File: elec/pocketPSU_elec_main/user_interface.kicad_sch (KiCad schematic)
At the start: 0 parts

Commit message: added user interface elements
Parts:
- added C1: C_Small, symbol Device:C_Small
- added C2, C3: 10nF, symbol Device:C_Small
- added J1: Conn_01x12_MountingPin, footprints:LCD-GMT020-02, symbol Connector_Generic_MountingPin:Conn_01x12_MountingPin
- added KEY1, KEY2, KEY3: TS3325A 250GF 025, footprints:KEY-SMD_4P-L3.1-W3.1-P2.00-LS4.0, symbol footprints:TS3325A250GF025
- added R1: 4.7R, symbol Device:R_Small
- added R2, R3, R4, R5, R6, R7, R8, R9: 10K, symbol Device:R_Small
- added SW1: EC11E09244BS, footprints:SW-TH_EC11XXXXXXXX, symbol footprints:EC11E09244BS
- added U1: 2N7002_C5224215, footprints:SOT-23-3_L3.0-W1.6-P1.90-LS2.8-BR, symbol footprints:2N7002_C5224215
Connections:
- new net: C2.1, R2.2, R3.2, SW1.A
- new net: C3.1, R4.2, R5.1, SW1.B
- new net: R1.2, U1.3 (D)
- new net +3.3V: C1.1, J1.3 (Pin_3), J1.4 (Pin_4), R2.1, R4.1, R6.1, R7.1, R8.1, R9.1
- new net BT_1: KEY1.1, KEY1.2, R7.2
- new net BT_2: KEY2.1, KEY2.2, R8.2
- new net BT_3: KEY3.1, KEY3.2, R9.2
- new net ENCODER_A: R3.1
- new net ENCODER_B: R5.2
- new net ENCODER_BT: R6.2, SW1.D
- new net GND: C1.2, C2.2, C3.2, J1.1 (Pin_1), J1.12 (Pin_12), J1.5 (Pin_5), J1.6 (Pin_6), KEY1.3, KEY1.4, KEY1.5, KEY1.6, KEY2.3, KEY2.4, KEY2.5, KEY2.6, KEY3.3, KEY3.4, KEY3.5, KEY3.6, SW1.6, SW1.7, SW1.C, SW1.E, U1.2 (S)
- new net LEDK: J1.2 (Pin_2), R1.1
- new net SCREEN_BACKLIGHT_EN: U1.1 (G)
- new net SPI_CS: J1.8 (Pin_8)
- new net SPI_DC: J1.7 (Pin_7)
- new net SPI_MOSI: J1.10 (Pin_10)
- new net SPI_RESET: J1.11 (Pin_11)
- new net SPI_SCK: J1.9 (Pin_9)

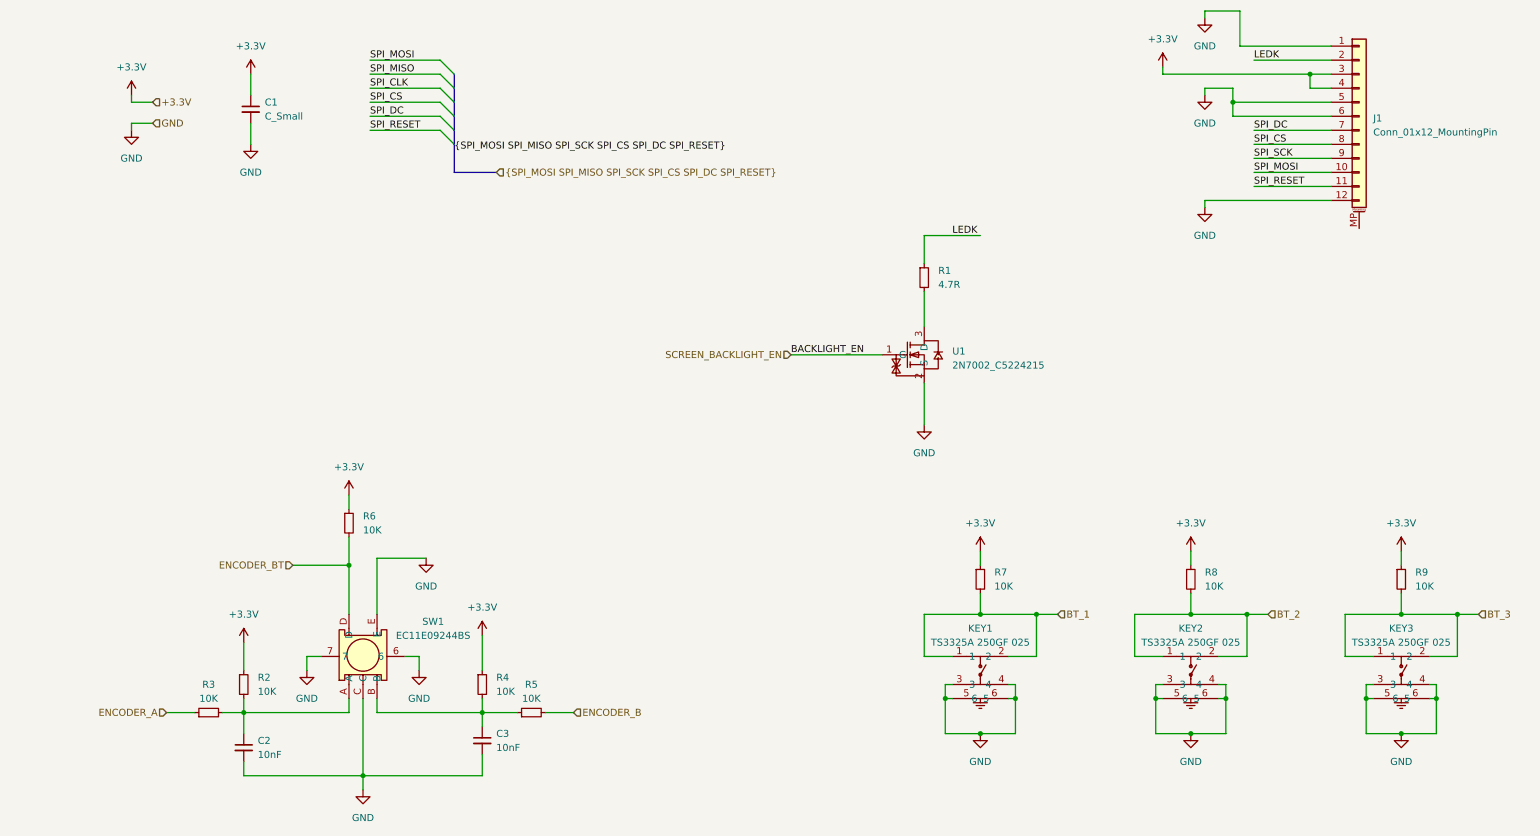
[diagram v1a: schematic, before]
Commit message: add button, deglitch
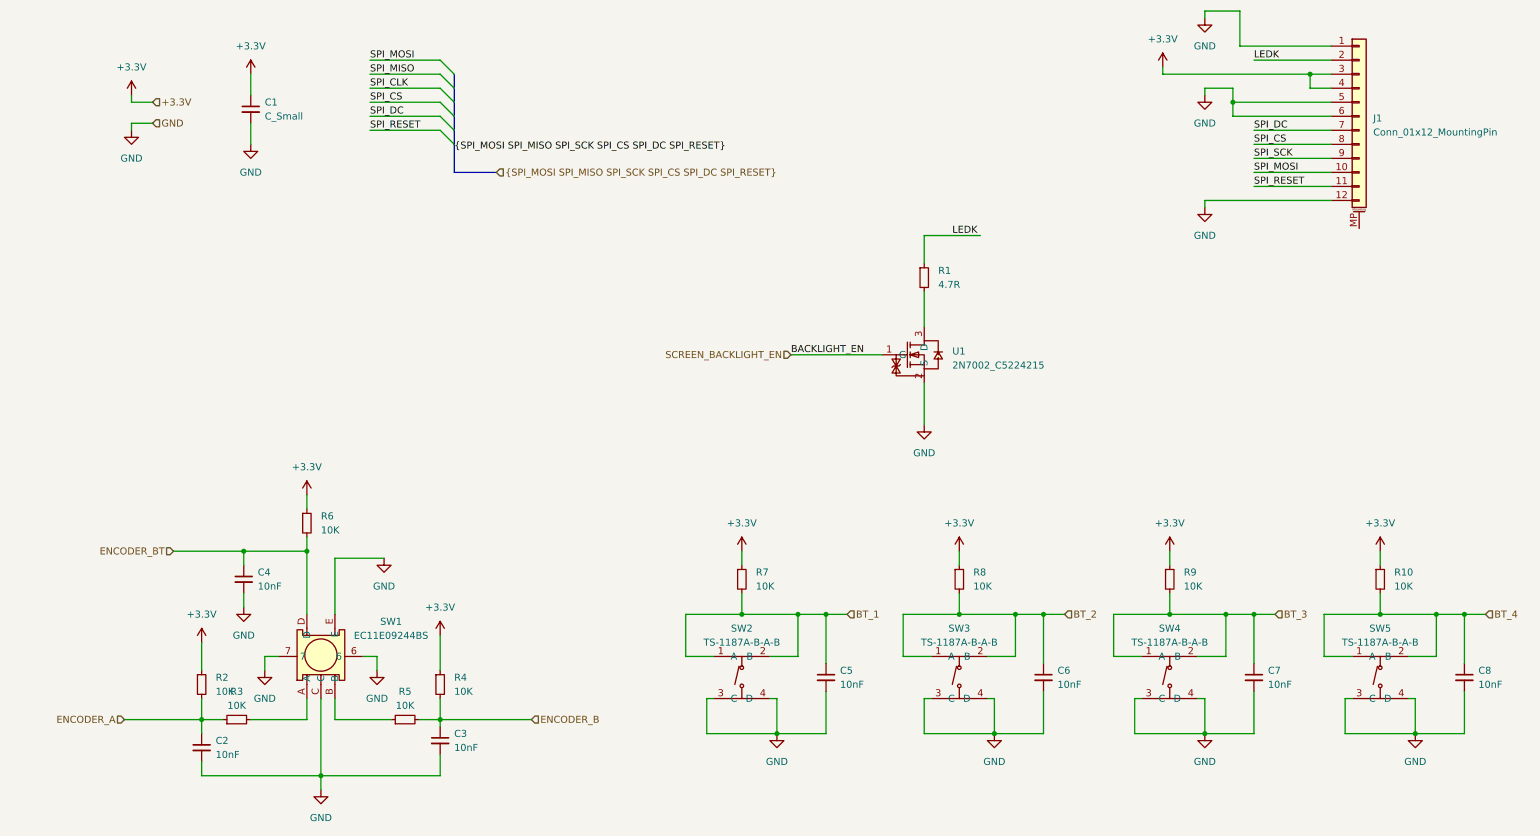
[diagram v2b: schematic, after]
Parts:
- removed KEY1, KEY2, KEY3: TS3325A 250GF 025, footprints:KEY-SMD_4P-L3.1-W3.1-P2.00-LS4.0, symbol footprints:TS3325A250GF025
- added C4, C5, C6, C7, C8: 10nF, symbol Device:C_Small
- added R10: 10K, symbol Device:R_Small
- added SW2, SW3, SW4, SW5: TS-1187A-B-A-B, footprints:SW-SMD_4P-L5.1-W5.1-P3.70-LS6.5-TL-2, symbol footprints:TS-1187A-B-A-B
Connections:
- net +3.3V: now also R10.1
- net BT_1: now also C5.1, SW2.1 (A), SW2.2 (B)
- net BT_2: now also C6.1, SW3.1 (A), SW3.2 (B)
- net BT_3: now also C7.1, SW4.1 (A), SW4.2 (B)
- net ENCODER_A: now also C2.1, R2.2
- net ENCODER_B: now also C3.1, R4.2
- net ENCODER_BT: now also C4.1
- net GND: now also C4.2, C5.2, C6.2, C7.2, C8.2, SW2.3 (C), SW2.4 (D), SW3.3 (C), SW3.4 (D), SW4.3 (C), SW4.4 (D), SW5.3 (C), SW5.4 (D)
- net at R3.2, SW1.A: no longer C2.1, R2.2
- net at R5.1, SW1.B: no longer C3.1, R4.2
- new net BT_4: C8.1, R10.2, SW5.1 (A), SW5.2 (B)
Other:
- moved on the sheet: C2, C3, R2, R3, R4, R5, R6, R7, SW1

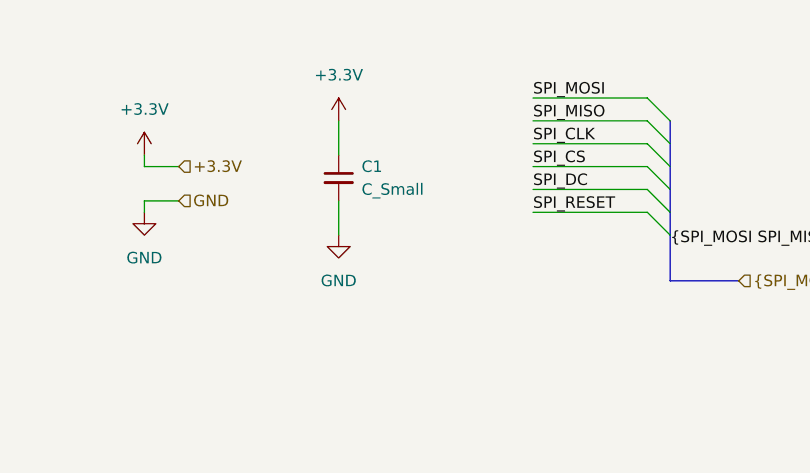
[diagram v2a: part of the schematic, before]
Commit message: add value to bypass cap
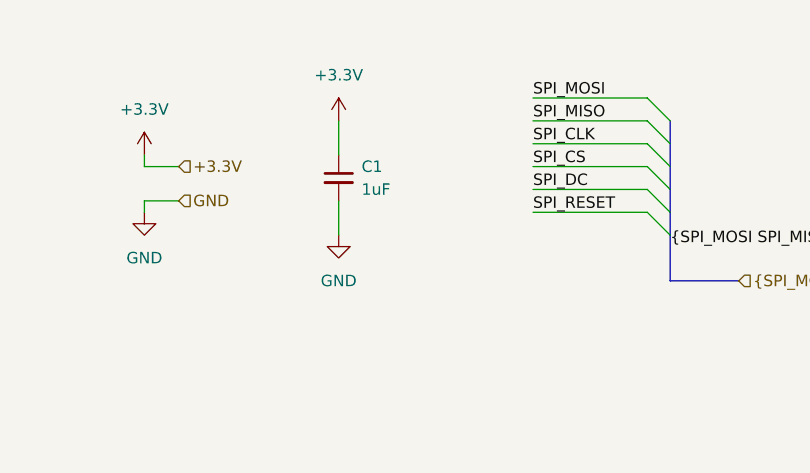
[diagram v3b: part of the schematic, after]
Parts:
- C1: value C_Small -> 1uF
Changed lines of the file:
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@@
 			)
 		)
-		(property "Value" "C_Small"
+		(property "Value" "1uF"
 			(at 57.15 41.9162 0)
 			(effects

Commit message: add esp32 micro
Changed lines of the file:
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@@
 	)
 	(hierarchical_label "ENCODER_BT"
-		(shape input)
+		(shape output)
 		(at 40.64 120.65 180)
 		(fields_autoplaced yes)
@@
 	)
 	(hierarchical_label "ENCODER_A"
-		(shape input)
+		(shape output)
 		(at 31.75 151.13 180)
 		(fields_autoplaced yes)
@@
 	)
 	(hierarchical_label "BT_3"
-		(shape input)
+		(shape output)
 		(at 240.03 132.08 0)
 		(fields_autoplaced yes)
@@
 	)
 	(hierarchical_label "BT_1"
-		(shape input)
+		(shape output)
 		(at 162.56 132.08 0)
 		(fields_autoplaced yes)
@@
 	)
 	(hierarchical_label "ENCODER_B"
-		(shape input)
+		(shape output)
 		(at 105.41 151.13 0)
 		(fields_autoplaced yes)
@@
 	)
 	(hierarchical_label "BT_4"
-		(shape input)
+		(shape output)
 		(at 278.13 132.08 0)
 		(fields_autoplaced yes)
@@
 	)
 	(hierarchical_label "BT_2"
-		(shape input)
+		(shape output)
 		(at 201.93 132.08 0)
 		(fields_autoplaced yes)

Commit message: preliminary layout
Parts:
- C1: footprint (none) -> Resistor_SMD:R_0805_2012Metric
- C2, C3, C4, C5, C6, C7, C8: footprint (none) -> Capacitor_SMD:C_0402_1005Metric
- R1, R10, R2, R3, R4, R5, R6, R7, R8, R9: footprint (none) -> Resistor_SMD:R_0402_1005Metric
- renumbered SW3 to BTDOWN1, SW5 to BTON1, SW4 to BTSELECT1, SW2 to BTUP1
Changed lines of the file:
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@@
 			)
 		)
-		(property "Footprint" ""
+		(property "Footprint" "Resistor_SMD:R_0805_2012Metric"
 			(at 54.61 40.64 0)
 			(effects
@@
 			)
 		)
-		(property "Footprint" ""
+		(property "Footprint" "Capacitor_SMD:C_0402_1005Metric"
 			(at 236.22 143.51 0)
 			(effects
@@
 			)
 		)
-		(property "Footprint" ""
+		(property "Footprint" "Resistor_SMD:R_0402_1005Metric"
 			(at 45.72 144.78 0)
 			(effects
@@
 			)
 		)
-		(property "Footprint" ""
+		(property "Footprint" "Resistor_SMD:R_0402_1005Metric"
 			(at 82.55 151.13 0)
 			(effects
@@
 			)
 		)
-		(property "Footprint" ""
+		(property "Footprint" "Resistor_SMD:R_0402_1005Metric"
 			(at 220.98 125.73 0)
 			(effects
@@
 		(dnp no)
 		(fields_autoplaced yes)
-		(property "Reference" "SW5"
+		(property "Reference" "BTON1"
 			(at 259.08 134.62 0)
 			(effects
@@
 			(project "pocketPSU_elec_main"
 				(path "/439011d5-4dd5-4d65-a9bd-b0be402d54a5/cbe29d96-4bd9-4dd2-be02-96003f32f1da"
-					(reference "SW5")
+					(reference "BTON1")
 					(unit 1)
 				)
@@
 			)
 		)
-		(property "Footprint" ""
+		(property "Footprint" "Capacitor_SMD:C_0402_1005Metric"
 			(at 198.12 143.51 0)
 			(effects
@@
 		(dnp no)
 		(fields_autoplaced yes)
-		(property "Reference" "SW3"
+		(property "Reference" "BTDOWN1"
 			(at 182.88 134.62 0)
 			(effects
@@
 			(project "pocketPSU_elec_main"
 				(path "/439011d5-4dd5-4d65-a9bd-b0be402d54a5/cbe29d96-4bd9-4dd2-be02-96003f32f1da"
-					(reference "SW3")
+					(reference "BTDOWN1")
 					(unit 1)
 				)
@@
 			)
 		)
-		(property "Footprint" ""
+		(property "Footprint" "Capacitor_SMD:C_0402_1005Metric"
 			(at 158.75 143.51 0)
 			(effects
@@
 			)
 		)
-		(property "Footprint" ""
+		(property "Footprint" "Capacitor_SMD:C_0402_1005Metric"
 			(at 88.9 154.94 0)
 			(effects
@@
 			)
 		)
-		(property "Footprint" ""
+		(property "Footprint" "Resistor_SMD:R_0402_1005Metric"
 			(at 64.77 115.57 0)
 			(effects
@@
 			)
 		)
-		(property "Footprint" ""
+		(property "Footprint" "Capacitor_SMD:C_0402_1005Metric"
 			(at 53.34 125.73 0)
 			(effects
@@
 			)
 		)
-		(property "Footprint" ""
+		(property "Footprint" "Resistor_SMD:R_0402_1005Metric"
 			(at 176.53 71.12 0)
 			(effects
@@
 			)
 		)
-		(property "Footprint" ""
+		(property "Footprint" "Resistor_SMD:R_0402_1005Metric"
 			(at 143.51 125.73 0)
 			(effects
@@
 			)
 		)
-		(property "Footprint" ""
+		(property "Footprint" "Resistor_SMD:R_0402_1005Metric"
 			(at 88.9 144.78 0)
 			(effects
@@
 		(dnp no)
 		(fields_autoplaced yes)
-		(property "Reference" "SW4"
+		(property "Reference" "BTSELECT1"
 			(at 220.98 134.62 0)
 			(effects
@@
 			(project "pocketPSU_elec_main"
 				(path "/439011d5-4dd5-4d65-a9bd-b0be402d54a5/cbe29d96-4bd9-4dd2-be02-96003f32f1da"
-					(reference "SW4")
+					(reference "BTSELECT1")
 					(unit 1)
 				)
@@
 			)
 		)
-		(property "Footprint" ""
+		(property "Footprint" "Resistor_SMD:R_0402_1005Metric"
 			(at 182.88 125.73 0)
 			(effects
@@
 			)
 		)
-		(property "Footprint" ""
+		(property "Footprint" "Capacitor_SMD:C_0402_1005Metric"
 			(at 45.72 156.21 0)
 			(effects
@@
 			)
 		)
-		(property "Footprint" ""
+		(property "Footprint" "Resistor_SMD:R_0402_1005Metric"
 			(at 259.08 125.73 0)
 			(effects
@@
 			)
 		)
-		(property "Footprint" ""
+		(property "Footprint" "Resistor_SMD:R_0402_1005Metric"
 			(at 52.07 151.13 0)
 			(effects
@@
 		(dnp no)
 		(fields_autoplaced yes)
-		(property "Reference" "SW2"
+		(property "Reference" "BTUP1"
 			(at 143.51 134.62 0)
 			(effects
@@
 			(project "pocketPSU_elec_main"
 				(path "/439011d5-4dd5-4d65-a9bd-b0be402d54a5/cbe29d96-4bd9-4dd2-be02-96003f32f1da"
-					(reference "SW2")
+					(reference "BTUP1")
 					(unit 1)
 				)
@@
 			)
 		)
-		(property "Footprint" ""
+		(property "Footprint" "Capacitor_SMD:C_0402_1005Metric"
 			(at 274.32 143.51 0)
 			(effects

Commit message: add usb coms chip
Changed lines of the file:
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@@
-	(wire
-		(pts
-			(xy 33.02 43.18) (xy 36.83 43.18)
-		)
-		(stroke
-			(width 0)
-			(type default)
-		)
-	)
 	(wire
 		(pts
@@
 	(wire
 		(pts
-			(xy 33.02 39.37) (xy 36.83 39.37)
-		)
-		(stroke
-			(width 0)
-			(type default)
-		)
-	)
-	(wire
-		(pts
 			(xy 158.75 132.08) (xy 162.56 132.08)
 		)
@@
 	(wire
 		(pts
-			(xy 33.02 44.45) (xy 33.02 43.18)
-		)
-		(stroke
-			(width 0)
-			(type default)
-		)
-	)
-	(wire
-		(pts
 			(xy 45.72 137.16) (xy 45.72 142.24)
 		)
@@
 		(pts
 			(xy 264.16 139.7) (xy 269.24 139.7)
-		)
-		(stroke
-			(width 0)
-			(type default)
-		)
-	)
-	(wire
-		(pts
-			(xy 33.02 38.1) (xy 33.02 39.37)
 		)
 		(stroke
@@
 		(shape output)
 		(at 240.03 132.08 0)
-		(fields_autoplaced yes)
-		(effects
-			(font
-				(size 1.27 1.27)
-			)
-			(justify left)
-		)
-	)
-	(hierarchical_label "GND"
-		(shape input)
-		(at 36.83 43.18 0)
-		(fields_autoplaced yes)
-		(effects
-			(font
-				(size 1.27 1.27)
-			)
-			(justify left)
-		)
-	)
-	(hierarchical_label "+3.3V"
-		(shape input)
-		(at 36.83 39.37 0)
 		(fields_autoplaced yes)
 		(effects
@@
 	)
 	(symbol
-		(lib_id "power:+3.3V")
-		(at 33.02 38.1 0)
-		(unit 1)
-		(exclude_from_sim no)
-		(in_bom yes)
-		(on_board yes)
-		(dnp no)
-		(fields_autoplaced yes)
-		(property "Reference" "#PWR09"
-			(at 33.02 41.91 0)
-			(effects
-				(font
-					(size 1.27 1.27)
-				)
-				(hide yes)
-			)
-		)
-		(property "Value" "+3.3V"
-			(at 33.02 33.02 0)
-			(effects
-				(font
-					(size 1.27 1.27)
-				)
-			)
-		)
-		(property "Footprint" ""
-			(at 33.02 38.1 0)
-			(effects
-				(font
-					(size 1.27 1.27)
-				)
-				(hide yes)
-			)
-		)
-		(property "Datasheet" ""
-			(at 33.02 38.1 0)
-			(effects
-				(font
-					(size 1.27 1.27)
-				)
-				(hide yes)
-			)
-		)
-		(property "Description" "Power symbol creates a global label with name \"+3.3V\""
-			(at 33.02 38.1 0)
-			(effects
-				(font
-					(size 1.27 1.27)
-				)
-				(hide yes)
-			)
-		)
-		(pin "1"
-		)
-		(instances
-			(project "pocketPSU_elec_main"
-				(path "/439011d5-4dd5-4d65-a9bd-b0be402d54a5/cbe29d96-4bd9-4dd2-be02-96003f32f1da"
-					(reference "#PWR09")
-					(unit 1)
-				)
-			)
-		)
-	)
-	(symbol
 		(lib_id "Device:R_Small")
 		(at 45.72 144.78 0)
@@
 					(unit 1)
 				)
-			)
-		)
-	)
-	(symbol
-		(lib_id "power:GND")
-		(at 33.02 44.45 0)
-		(unit 1)
-		(exclude_from_sim no)
-		(in_bom yes)
-		(on_board yes)
-		(dnp no)
-		(fields_autoplaced yes)
-		(property "Reference" "#PWR08"
-			(at 33.02 50.8 0)
-			(effects
-				(font
-					(size 1.27 1.27)
-				)
-				(hide yes)
-			)
-		)
-		(property "Value" "GND"
-			(at 33.02 49.53 0)
-			(effects
-				(font
-					(size 1.27 1.27)
-				)
-			)
-		)
-		(property "Footprint" ""
-			(at 33.02 44.45 0)
-			(effects
-				(font
-					(size 1.27 1.27)
-				)
-				(hide yes)
-			)
-		)
-		(property "Datasheet" ""
-			(at 33.02 44.45 0)
-			(effects
-				(font
-					(size 1.27 1.27)
-				)
-				(hide yes)
-			)
-		)
-		(property "Description" "Power symbol creates a global label with name \"GND\" , ground"
-			(at 33.02 44.45 0)
-			(effects
-				(font
-					(size 1.27 1.27)
-				)
-				(hide yes)
-			)
-		)
-		(pin "1"
-		)
-		(instances
-			(project "pocketPSU_elec_main"
-				(path "/439011d5-4dd5-4d65-a9bd-b0be402d54a5/cbe29d96-4bd9-4dd2-be02-96003f32f1da"
-					(reference "#PWR08")
-					(unit 1)
-				)

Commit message: fix caps values, rework layout
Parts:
- removed J1: Conn_01x12_MountingPin, footprints:LCD-GMT020-02, symbol Connector_Generic_MountingPin:Conn_01x12_MountingPin
- added J3: Conn_01x12_Pin, footprints:LCD-GMT020-02, symbol Connector:Conn_01x12_Pin
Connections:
- net +3.3V: now also J3.10 (Pin_10), J3.9 (Pin_9)
- net GND: now also J3.1 (Pin_1), J3.12 (Pin_12), J3.7 (Pin_7), J3.8 (Pin_8)
- net LEDK: now also J3.11 (Pin_11)
- net SPI_CS: now also J3.5 (Pin_5)
- net SPI_DC: now also J3.6 (Pin_6)
- net SPI_MOSI: now also J3.3 (Pin_3)
- net SPI_RESET: now also J3.2 (Pin_2)
- net SPI_SCK: now also J3.4 (Pin_4)
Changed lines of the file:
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@@
+	)
+	(symbol
+		(lib_id "Connector:Conn_01x12_Pin")
+		(at 255.27 44.45 180)
+		(unit 1)
+		(exclude_from_sim no)
+		(in_bom yes)
+		(on_board yes)
+		(dnp no)
+		(fields_autoplaced yes)
+		(property "Reference" "J3"
+			(at 256.54 41.9099 0)
+			(effects
+				(font
+					(size 1.27 1.27)
+				)
+				(justify right)
+			)
+		)
+		(property "Value" "Conn_01x12_Pin"
+			(at 256.54 44.4499 0)
+			(effects
+				(font
+					(size 1.27 1.27)
+				)
+				(justify right)
+			)
+		)
+		(property "Footprint" "footprints:LCD-GMT020-02"
+			(at 255.27 44.45 0)
+			(effects
+				(font
+					(size 1.27 1.27)
+				)
+				(hide yes)
+			)
+		)
+		(property "Datasheet" "~"
+			(at 255.27 44.45 0)
+			(effects
+				(font
+					(size 1.27 1.27)
+				)
+				(hide yes)
+			)
+		)
+		(property "Description" "Generic connector, single row, 01x12, script generated"
+			(at 255.27 44.45 0)
+			(effects
+				(font
+					(size 1.27 1.27)
+				)
+				(hide yes)
+			)
+		)
+		(pin "12"
+		)
+		(pin "3"
+		)
+		(pin "4"
+		)
+		(pin "1"
+		)
+		(pin "6"
+		)
+		(pin "7"
+		)
+		(pin "10"
+		)
+		(pin "5"
+		)
+		(pin "8"
+		)
+		(pin "9"
+		)
+		(pin "11"
+		)
+		(pin "2"
+		)
+		(instances
+			(project "pocketPSU_elec_main"
+				(path "/439011d5-4dd5-4d65-a9bd-b0be402d54a5/cbe29d96-4bd9-4dd2-be02-96003f32f1da"
+					(reference "J3")
+					(unit 1)
+				)
+			)
+		)
 	)
 	(symbol
@@
 					(unit 1)
 				)
-			)
-		)
-	)
-	(symbol
-		(lib_id "Connector_Generic_MountingPin:Conn_01x12_MountingPin")
-		(at 255.27 41.91 0)
-		(unit 1)
-		(exclude_from_sim no)
-		(in_bom yes)
-		(on_board yes)
-		(dnp no)
-		(fields_autoplaced yes)
-		(property "Reference" "J1"
-			(at 257.81 42.2655 0)
-			(effects
-				(font
-					(size 1.27 1.27)
-				)
-				(justify left)
-			)
-		)
-		(property "Value" "Conn_01x12_MountingPin"
-			(at 257.81 44.8055 0)
-			(effects
-				(font
-					(size 1.27 1.27)
-				)
-				(justify left)
-			)
-		)
-		(property "Footprint" "footprints:LCD-GMT020-02"
-			(at 255.27 41.91 0)
-			(effects
-				(font
-					(size 1.27 1.27)
-				)
-				(hide yes)
-			)
-		)
-		(property "Datasheet" "~"
-			(at 255.27 41.91 0)
-			(effects
-				(font
-					(size 1.27 1.27)
-				)
-				(hide yes)
-			)
-		)
-		(property "Description" "Generic connectable mounting pin connector, single row, 01x12, script generated (kicad-library-utils/schlib/autogen/connector/)"
-			(at 255.27 41.91 0)
-			(effects
-				(font
-					(size 1.27 1.27)
-				)
-				(hide yes)
-			)
-		)
-		(pin "5"
-		)
-		(pin "12"
-		)
-		(pin "MP"
-		)
-		(pin "6"
-		)
-		(pin "8"
-		)
-		(pin "3"
-		)
-		(pin "11"
-		)
-		(pin "10"
-		)
-		(pin "4"
-		)
-		(pin "2"
-		)
-		(pin "9"
-		)
-		(pin "7"
-		)
-		(pin "1"
-		)
-		(instances
-			(project "pocketPSU_elec_main"
-				(path "/439011d5-4dd5-4d65-a9bd-b0be402d54a5/cbe29d96-4bd9-4dd2-be02-96003f32f1da"
-					(reference "J1")
-					(unit 1)
-				)
